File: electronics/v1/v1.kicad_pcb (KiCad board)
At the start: 2 copper layers, 25.4 x 25.4 mm, 52 parts, among them J1 AVR-ISP-6, J2 SENSE_ELECTRODE, U1 ATmega328P-MMH, U2 MCP16251T-I/CH, U3 AT42QT1010-TSHR, Y1 8MHz

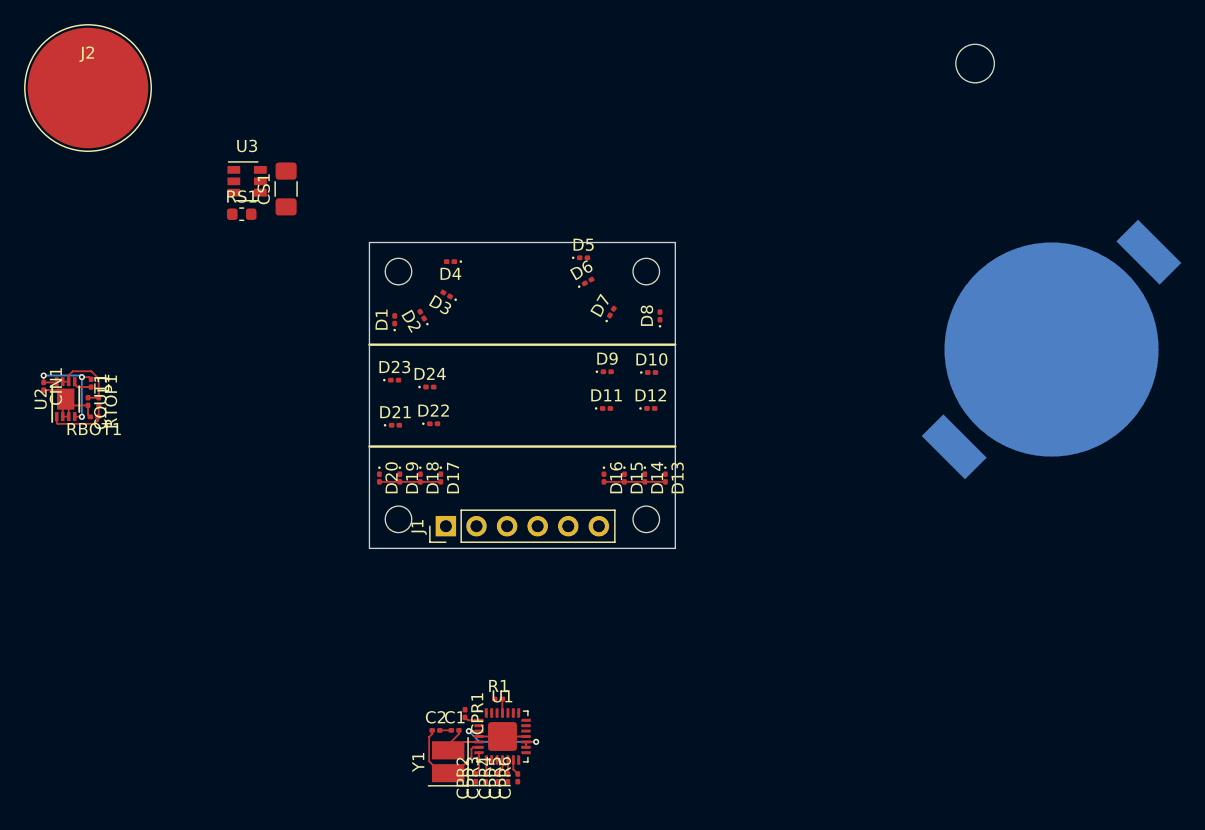
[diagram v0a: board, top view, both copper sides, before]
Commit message: Add reference backup layout for 0201 mistake, Resolve issues, & Finish component layout.
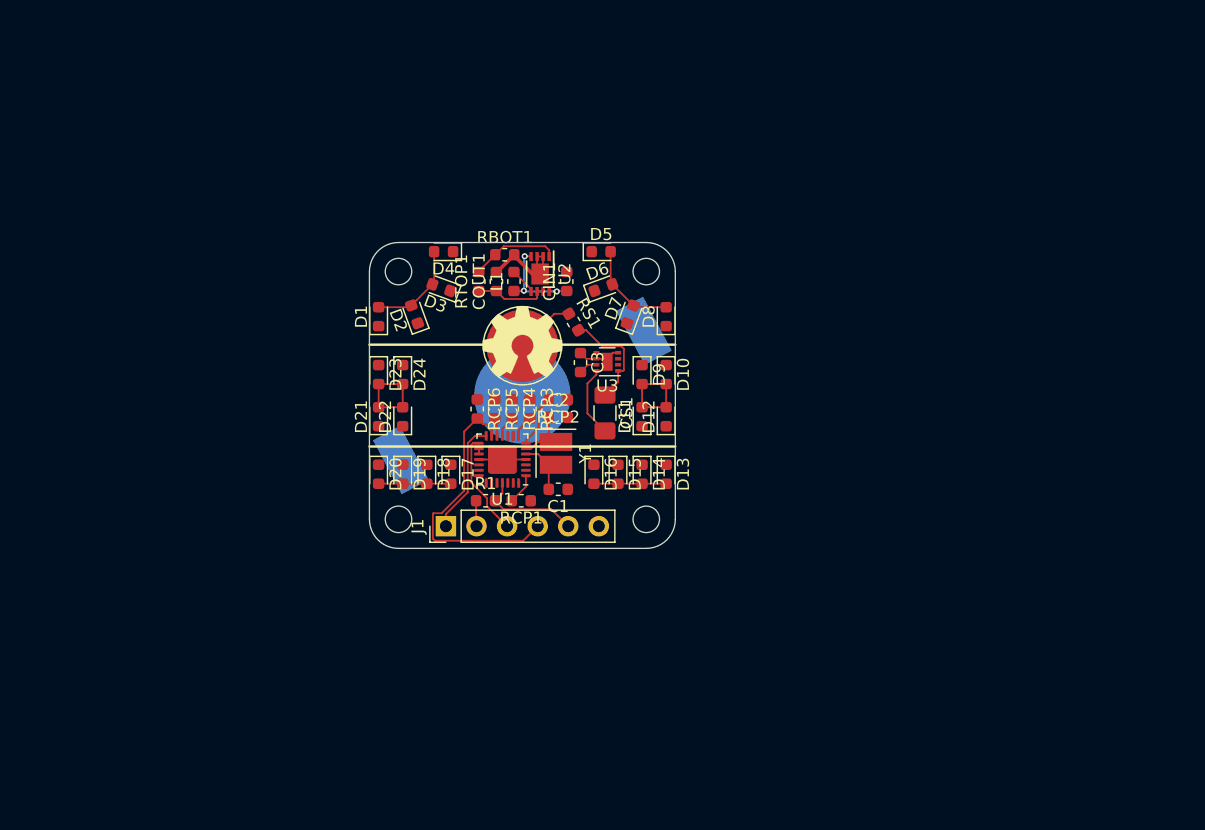
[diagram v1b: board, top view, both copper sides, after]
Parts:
- removed CPR1, CPR2, CPR3, CPR4, CPR5, CPR6: R, Resistor_SMD:R_0201_0603Metric
- removed the hole at (232.8, 100.2)
- added C3: 0.1uF, Capacitor_SMD:C_0603_1608Metric, F.Cu at (200.0, 125.0)
- added RCP1: R, Resistor_SMD:R_0603_1608Metric, F.Cu at (195.1, 136.5)
- added RCP2: R, Resistor_SMD:R_0603_1608Metric, F.Cu at (198.2, 128.1)
- added RCP3: R, Resistor_SMD:R_0603_1608Metric, F.Cu at (195.8, 128.9)
- added RCP4: R, Resistor_SMD:R_0603_1608Metric, F.Cu at (194.4, 128.9)
- added RCP5: R, Resistor_SMD:R_0603_1608Metric, F.Cu at (192.9, 128.9)
- added RCP6: R, Resistor_SMD:R_0603_1608Metric, F.Cu at (191.4, 128.9)
- added REF**: OSHW-Symbol_6.7x6mm_SilkScreen, Symbol:OSHW-Symbol_6.7x6mm_SilkScreen, F.Cu at (195.2, 123.3)
- BT1: footprint BattHolder:BatteryHolder_LINX_BAT-HLD-001-SMT -> BattHolder:BatteryHolder_LINX_BAT-HLD-001-SMT_SOLDERPAD
- C1, C2, CIN1, COUT1: footprint Capacitor_SMD:C_0201_0603Metric -> Capacitor_SMD:C_0603_1608Metric
- D1, D10, D11, D12, D13, D14, D15, D16, D17, D18, D19, D2, D20, D21, D22, D23, D24, D3, D4, D5, D6, D7, D8, D9: footprint LED_SMD:LED_0201_0603Metric -> LED_SMD:LED_0603_1608Metric
- J2: footprint CapSense:CapSense_MaskedPad_D10.0mm -> CapSense:CapSense_MaskedPad_D6.0mm
- L1: footprint Inductor_SMD:L_0201_0603Metric -> Inductor_SMD:L_0603_1608Metric
- R1, RBOT1, RTOP1: footprint Resistor_SMD:R_0201_0603Metric -> Resistor_SMD:R_0603_1608Metric
- U3: value AT42QT1010-TSHR -> AT42QT1010-MAH; footprint Package_TO_SOT_SMD:SOT-23-6 -> AT42QT1010:DFN-8-1EP_2x2mm_P0.5mm_EP0.9x1.5mm
- moved CIN1 44.3 mm to (198.9, 118.3), turned to 90 degrees
- moved BT1 44.1 mm to (195.2, 127.8), turned to 28 degrees
- moved J2 41.9 mm to (195.2, 123.6)
- moved U2 40.7 mm to (196.7, 117.7), turned to 270 degrees
- moved RBOT1 36.7 mm to (193.7, 116.1), turned to 0 degrees
- moved L1 36.1 mm to (194.5, 118.3), turned to 90 degrees
- moved COUT1 35.3 mm to (193.0, 118.3), turned to 90 degrees
- moved U3 33.5 mm to (202.2, 125.0), turned to 180 degrees
- moved RTOP1 33.1 mm to (191.6, 118.3), turned to 90 degrees
- moved CS1 32.4 mm to (202.1, 129.2), turned to 270 degrees
- moved RS1 29.0 mm to (199.5, 121.7), turned to 300 degrees
- moved C2 27.9 mm to (198.2, 129.6)
- moved Y1 27.1 mm to (198.0, 132.6), turned to 270 degrees
- moved U1 23.0 mm to (193.5, 133.1), turned to 180 degrees
- moved C1 21.8 mm to (198.2, 135.6), turned to 180 degrees
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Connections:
- U1 pad 10: CAPSENSE -> Net-(U1-Pad10)
- U1 pad 21: Net-(U1-Pad21) -> CAPSENSE
- U3 pad 1: CAPSENSE -> Net-(CS1-Pad1)
- U3 pad 2: GND -> Net-(U3-Pad2)
- U3 pad 3: Net-(CS1-Pad1) -> Net-(U3-Pad3)
- U3 pad 4: Net-(CS1-Pad2) -> GND
- U3 pad 5: +3V3 -> CAPSENSE
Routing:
- net CP6: track 1.31 -> 23.3 mm
- net Net-(D1-Pad2): track 0.00 -> 16.1 mm
- net MISO: track 0.00 -> 9.42 mm
- net Net-(CS1-Pad1): track 0.00 -> 9.15 mm
- net SCK: track 0.00 -> 8.67 mm
- net Net-(D10-Pad2): track 0.00 -> 7.85 mm
- net Net-(D1-Pad1): track 0.00 -> 7.85 mm
- net RESET: track 1.17 -> 8.68 mm
- net Net-(CS1-Pad2): track 0.00 -> 5.91 mm
- net Net-(J2-Pad1): track 0.00 -> 4.96 mm
- net +3V3: track 14.5 -> 10.3 mm, vias 2 -> 0
- net Net-(C2-Pad1): track 8.51 -> 5.01 mm
- net GND: track 13.8 -> 16.9 mm
- net CP2: track 1.87 -> 4.39 mm
- net Net-(RBOT1-Pad1): track 5.38 -> 7.43 mm
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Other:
- outline, holes or cut-outs redrawn
- board text added: "Almost done. Track up LEDs, double check everything, and ground fill."
- board text removed: "Wearable Holes on Enclosure?"

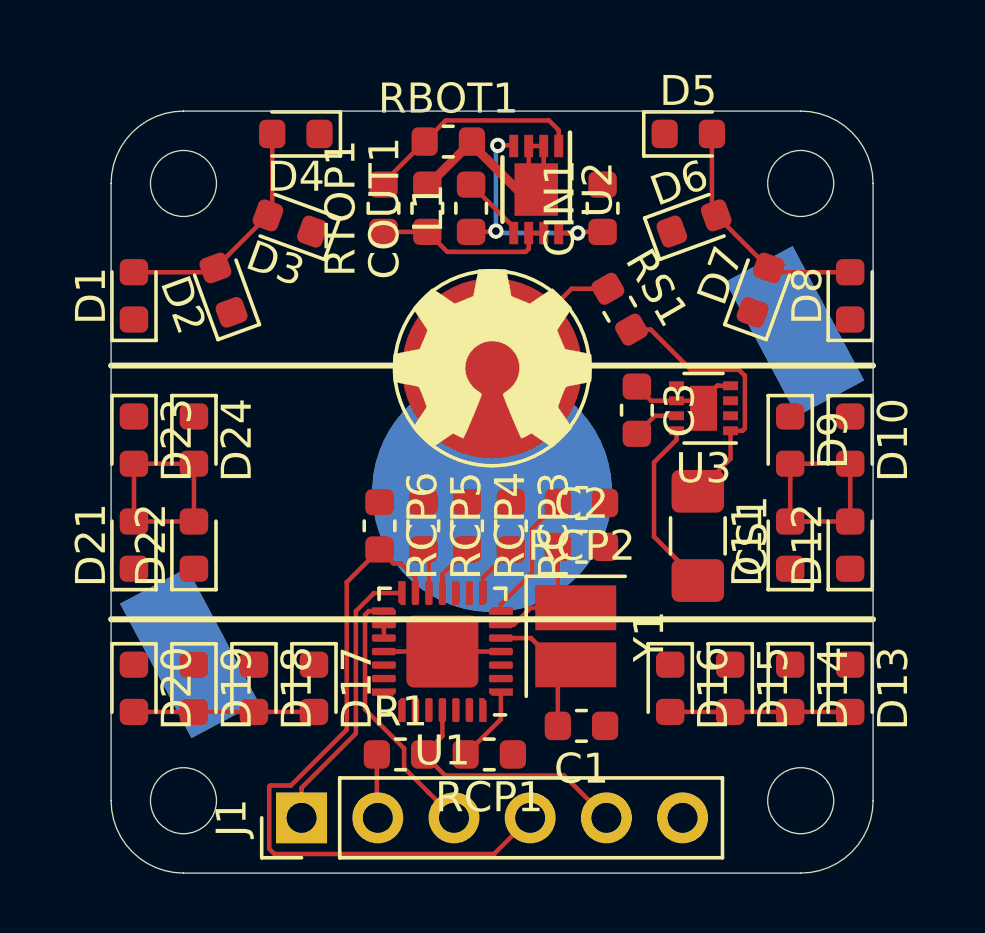
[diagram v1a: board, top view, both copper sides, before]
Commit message: Finish board routing, Add LED Charlieplexing truth table, Add jumpered electrode just in case
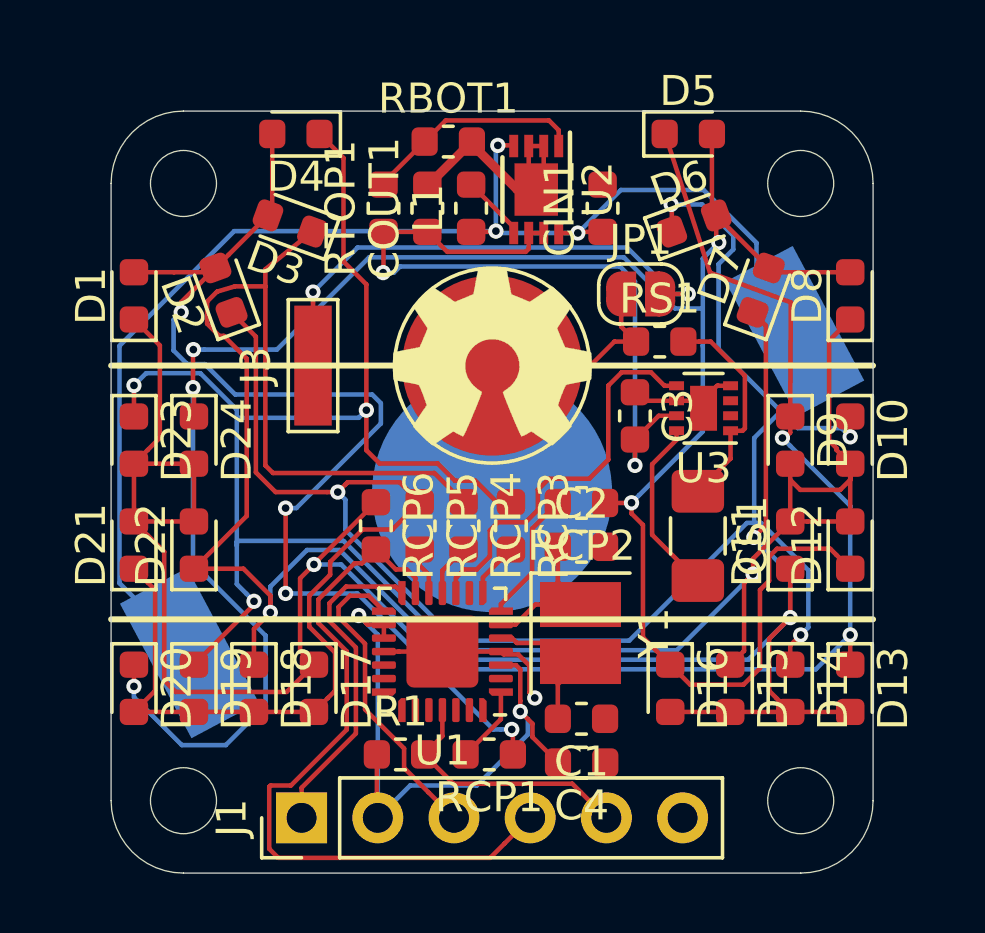
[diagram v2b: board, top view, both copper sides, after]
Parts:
- added C4: 0.1uF, Capacitor_SMD:C_0603_1608Metric, F.Cu at (198.2, 136.8)
- added J3: SENSE_ELECTRODE_AUX, CapSense:SMD_WIREPAD_4.0x1.25mm, F.Cu at (189.2, 123.5)
- added JP1: Jumper_NO_Small, Jumper:SolderJumper-2_P1.3mm_Open_RoundedPad1.0x1.5mm, F.Cu at (200.2, 121.2)
- moved RS1 1.72 mm to (200.8, 122.7), turned to 0 degrees
- moved C1 0.24 mm to (198.2, 135.3)
- moved C3 0.20 mm to (200.0, 125.2)
- moved Y1 0.19 mm to (198.1, 132.5)
- moved RCP4 0.12 mm to (194.2, 128.9)
- moved RCP5 0.12 mm to (192.8, 128.9)
- moved RCP6 0.12 mm to (191.3, 128.9)
- moved J2 0.09 mm to (195.2, 123.5)
- moved REF** 0.06 mm to (195.2, 123.3)
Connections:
- D12 pad 1: Net-(D1-Pad2) -> Net-(D12-Pad1)
- D16 pad 1: Net-(D1-Pad2) -> Net-(D12-Pad1)
- D20 pad 1: Net-(D1-Pad2) -> Net-(D12-Pad1)
- D24 pad 1: Net-(D1-Pad2) -> Net-(D12-Pad1)
- D5 pad 2: Net-(D1-Pad2) -> Net-(D12-Pad1)
- D6 pad 2: Net-(D1-Pad2) -> Net-(D12-Pad1)
- D7 pad 2: Net-(D1-Pad2) -> Net-(D12-Pad1)
- D8 pad 2: Net-(D1-Pad2) -> Net-(D12-Pad1)
- RCP2 pad 1: Net-(D1-Pad2) -> Net-(D12-Pad1)
- U1 pad 10: Net-(U1-Pad10) -> CAPSENSE
- U1 pad 21: CAPSENSE -> Net-(U1-Pad21)
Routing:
- net Net-(D12-Pad1): track 0.00 -> 75.7 mm, vias 0 -> 5
- net Net-(D11-Pad1): track 6.00 -> 76.7 mm, vias 0 -> 3
- net Net-(D10-Pad1): track 6.00 -> 74.7 mm, vias 0 -> 4
- net Net-(D10-Pad2): track 7.85 -> 75.4 mm, vias 0 -> 4
- net Net-(D1-Pad1): track 7.85 -> 72.0 mm, vias 0 -> 3
- net +3V3: track 10.3 -> 46.8 mm, vias 0 -> 4
- net Net-(BT1-Pad1): track 8.68 -> 44.8 mm
- net Net-(D1-Pad2): track 16.1 -> 37.1 mm, vias 0 -> 4
- net Net-(J3-Pad1): track 0.00 -> 17.2 mm, vias 0 -> 2
- net CAPSENSE: track 0.00 -> 13.2 mm
- net GND: track 16.9 -> 19.2 mm, vias 0 -> 1
- net Net-(J2-Pad1): track 4.96 -> 6.93 mm
- net Net-(CS1-Pad1): track 9.15 -> 7.26 mm
- net SCK: track 8.67 -> 10.5 mm
- net MISO: track 9.42 -> 11.0 mm
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
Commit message: Finalize PCB, Generate drill files for manufacturing, Begin lasercut enclosure design
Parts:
- J1: footprint Connector_PinHeader_2.54mm:PinHeader_1x06_P2.54mm_Vertical -> ISP_Connector:SIP-6_AVR_ISP
- moved D1 0.12 mm to (183.4, 121.2)
- moved D10 0.12 mm to (207.0, 126.0)
- moved D12 0.12 mm to (207.0, 129.5)
- moved D13 0.12 mm to (207.0, 134.3)
- moved D20 0.12 mm to (183.4, 134.3)
- moved D21 0.12 mm to (183.4, 129.5)
- moved D23 0.12 mm to (183.4, 126.0)
- moved D4 0.12 mm to (188.7, 115.9)
- moved D5 0.12 mm to (201.7, 115.9)
- moved D8 0.12 mm to (207.0, 121.2)
- renumbered RCP2 to 2, RCP3 to 3, RCP4 to 4, RCP5 to 5, RCP6 to 6
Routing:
- net GND: track 19.2 -> 45.3 mm, vias 1 -> 7
- net +3V3: track 46.8 -> 63.3 mm, vias 4 -> 5
- net Net-(D10-Pad2): track 75.4 -> 74.1 mm
- net Net-(D1-Pad1): track 72.0 -> 71.3 mm
- net Net-(RBOT1-Pad1): track 7.43 -> 7.55 mm, vias 0 -> 2
- added copper zone on B.Cu, net GND
- added copper zone on F.Cu, net GND
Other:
- board text added: "3V3"
- board text added: "AUX CAPSENSE"
- board text added: "Benjamin"
- board text added: "Broce"
- board text added: "Designed by"
- board text added: "GND"
- board text added: "MISO"
- board text added: "MOSI"
- board text added: "RCP"
- board text added: "RST"
- board text added: "SCK"
- board text removed: "Almost done. Track up LEDs, double check everything, and ground fill."
